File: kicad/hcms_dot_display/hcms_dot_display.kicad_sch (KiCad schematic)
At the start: 37 parts

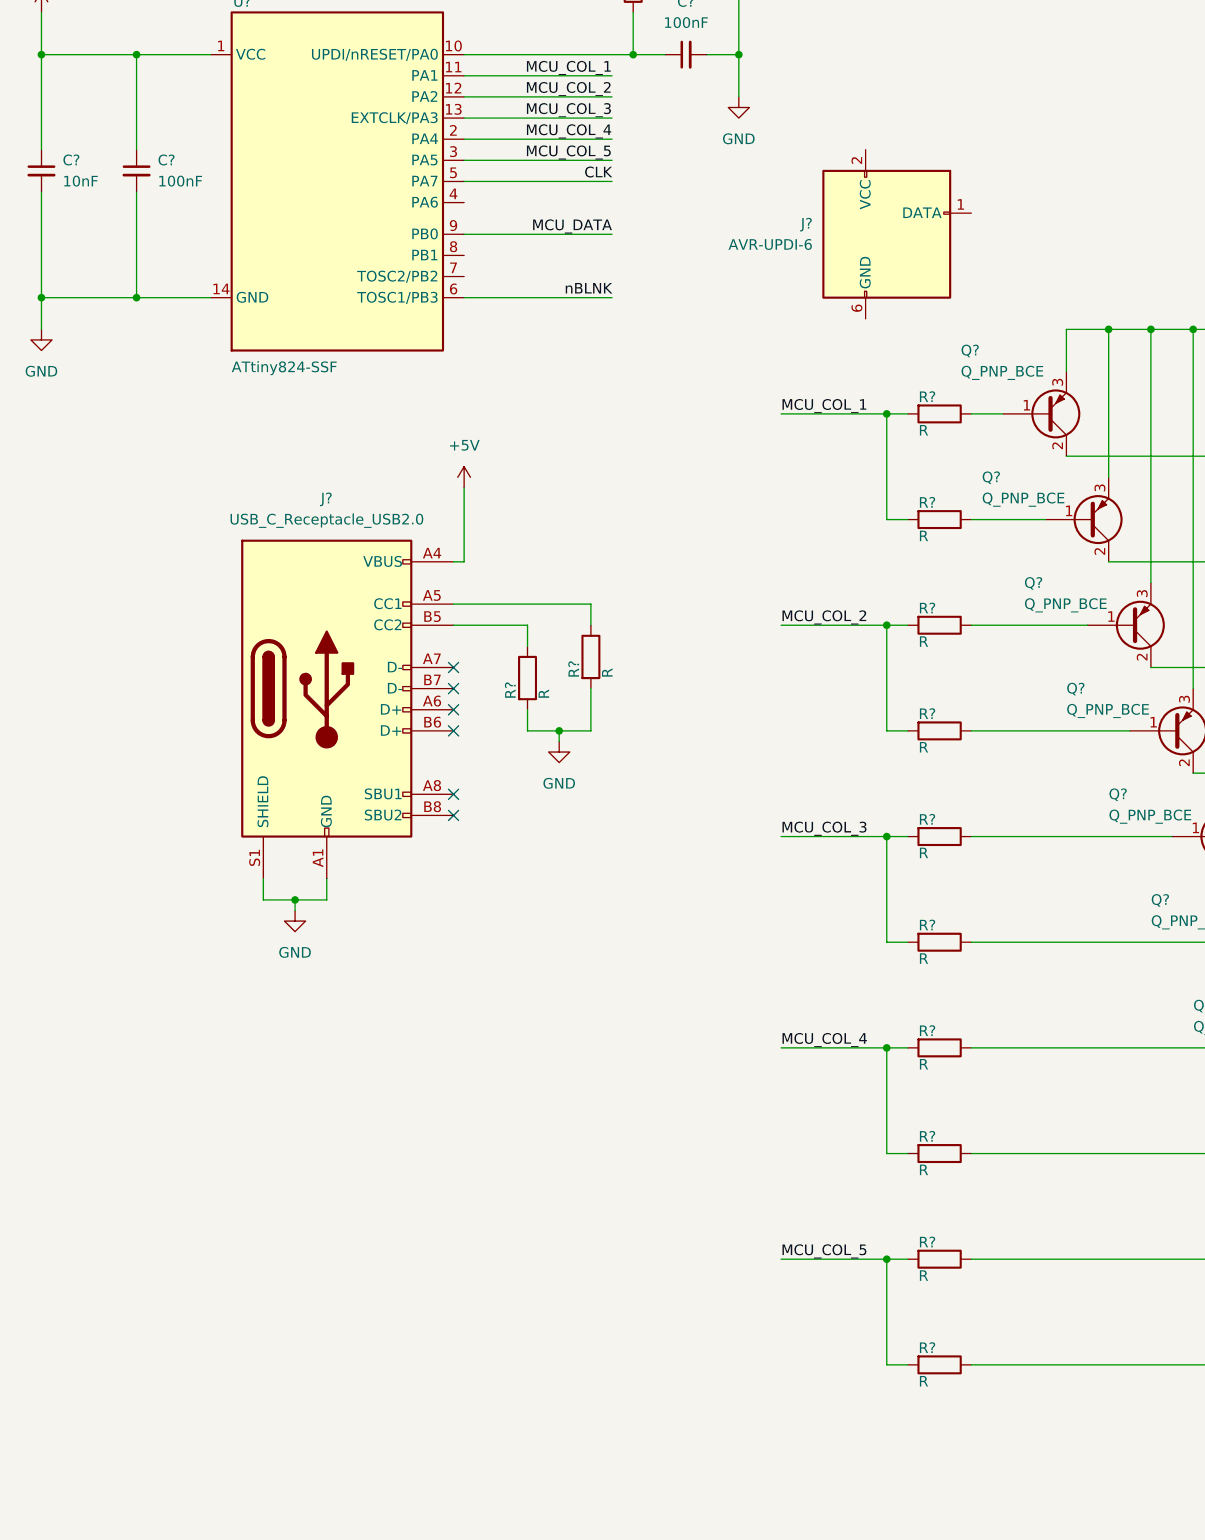
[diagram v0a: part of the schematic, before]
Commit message: battery dying
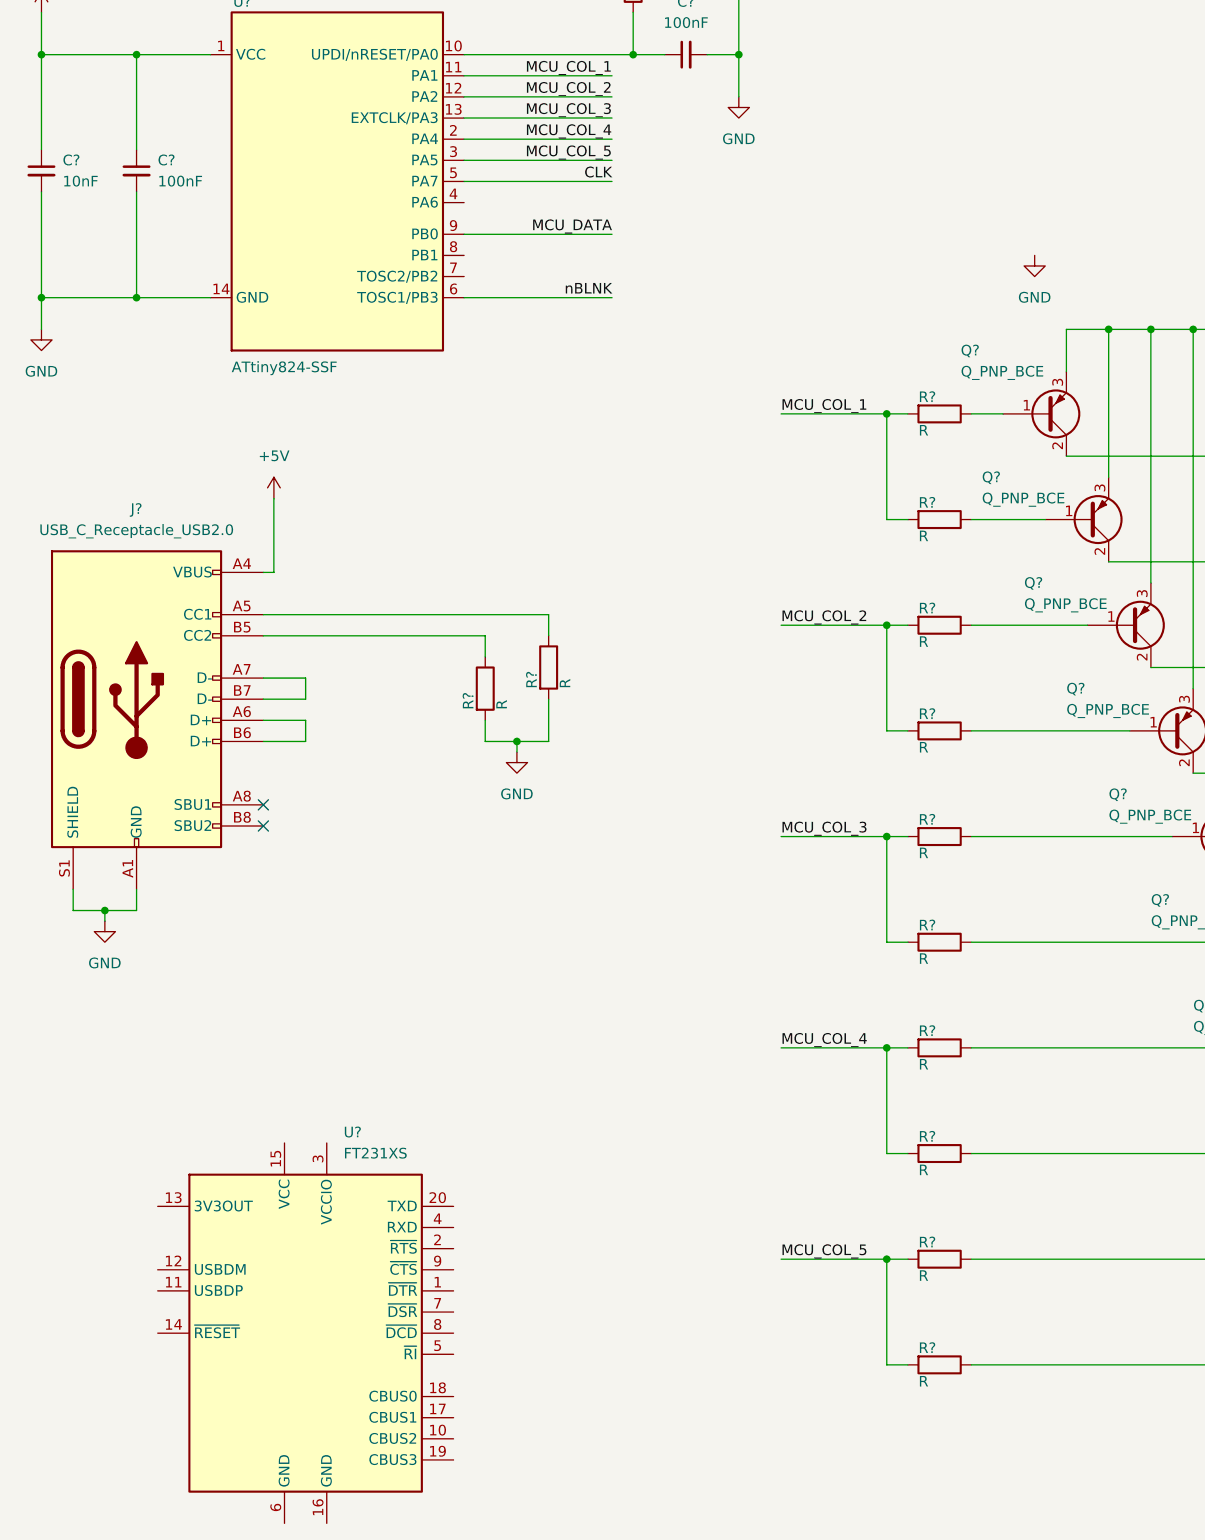
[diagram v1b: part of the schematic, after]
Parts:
- removed J?: AVR-UPDI-6, symbol Connector:AVR-UPDI-6
- added U?: FT231XS, Package_SO:SSOP-20_3.9x8.7mm_P0.635mm, symbol Interface_USB:FT231XS
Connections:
- net at J?.A6 (D+): now also J?.B6 (D+)
- net at J?.A7 (D-): now also J?.B7 (D-)
- no-connect marks 26 -> 22
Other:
- moved on the sheet: J?, R?

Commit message: aidan
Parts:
- removed Q? (x10): Q_PNP_BCE, symbol Device:Q_PNP_BCE
- removed R?: R, symbol Device:R
- added C? (x4): (no value), symbol Device:C_Small
- added C? (x2): 100nF, symbol Device:C_Small
- added J?: Conn_01x13, symbol Connector_Generic:Conn_01x13
- added Q? (x8): Q_PMOS_DSG, symbol Device:Q_PMOS_DSG
- added Q?: (no value), symbol Device:Q_PMOS_DSG
- added R? (x3): R, symbol Device:R
- added RV?: (no value), symbol Device:R_Potentiometer
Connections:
- net +5V: now also U?.15 (VCC), C?.1, C?.1, C?.1, J?.1 (Pin_1), Q?.2 (S), Q?.2 (S), Q?.2 (S), Q?.2 (S), Q?.2 (S), Q?.2 (S), Q?.2 (S), Q?.2 (S), Q?.2 (S), RV?.1
- net A_DATA: now also J?.9 (Pin_9)
- net B_DATA: now also J?.10 (Pin_10)
- net CLK: now also J?.8 (Pin_8)
- net COL_1A: now also Q?.1 (D)
- net COL_1B: now also Q?.1 (D)
- net COL_2A: now also Q?.1 (D)
- net COL_2B: now also Q?.1 (D)
- net COL_3A: now also Q?.1 (D)
- net COL_3B: now also Q?.1 (D)
- net COL_4A: now also Q?.1 (D)
- net COL_5A: now also Q?.1 (D)
- net DAISY_A_DATA: now also J?.11 (Pin_11)
- net DAISY_B_DATA: now also J?.12 (Pin_12)
- net GND: now also U?.16 (GND), U?.6 (GND), C?.2, C?.2, C?.2, C?.2, C?.2, C?.2, J?.13 (Pin_13), RV?.3
- net MCU_COL_1: now also J?.2 (Pin_2)
- net MCU_COL_2: now also J?.3 (Pin_3)
- net MCU_COL_3: now also J?.4 (Pin_4)
- net MCU_COL_4: now also J?.5 (Pin_5)
- net MCU_COL_5: now also J?.6 (Pin_6)
- net nBLNK: now also J?.7 (Pin_7)
- net at R?.1: now also Q?.3 (G) (x9)
- net at U?.11 (USBDP): now also R?.1
- net at U?.12 (USBDM): now also R?.1
- net +3V3: now reaches U?.13 (3V3OUT)
- net +3V3: now also U?.14 (~{RESET}), U?.3 (VCCIO), C?.1
- net at U?.20 (TXD): now also R?.2
- net UPDI: now reaches U?.4 (RXD)
- net UPDI: now also C?.1, R?.1, U?.10 (UPDI/nRESET/PA0), R?.1
- net POT: now reaches U?.4 (PA6)
- net POT: now also RV?.2
- net D+: now reaches J?.A6 (D+), J?.B6 (D+)
- net D+: now also C?.1, R?.2
- net D-: now reaches J?.A7 (D-), J?.B7 (D-)
- net D-: now also C?.1, R?.2
- no-connect marks 22 -> 32

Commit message: Reduce number of FETs, cleaned up schematic added some footprints, and starting routing
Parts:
- removed Q? (x4): Q_PMOS_DSG, symbol Device:Q_PMOS_DSG
- removed R? (x4): R, symbol Device:R
- added SW?: (no value), symbol Switch:SW_SPST
- D1: renamed from D?; value HCMS-272X -> (none)
- J1, J3: renamed from J?; value Conn_01x13 -> (none)
- J2: renamed from J?; value USB_C_Receptacle_USB2.0 -> (none)
- gave numbers to parts that had none: 33
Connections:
- net COL_1B is gone; now on net COL_1: D1.8 (COL_1)
- net COL_2B is gone; now on net COL_2: D1.2 (COL_2)
- net COL_3B is gone; now on net COL_3: D1.10 (COL_3)
- net COL_4B is gone; now on net COL_4: D1.4 (COL_4)
- net COL_5B is gone; now on net COL_5: D1.12 (COL_5)
- net +5V: now also SW?.2 (B); no longer J2.A4 (VBUS), J2.A9 (VBUS), J2.B4 (VBUS), J2.B9 (VBUS)
- net COL_1A renamed COL_1
- net COL_2A renamed COL_2
- net COL_3A renamed COL_3
- net COL_4A renamed COL_4
- net COL_5A renamed COL_5
- new net: J2.A4 (VBUS), J2.A9 (VBUS), J2.B4 (VBUS), J2.B9 (VBUS), SW?.1 (A)
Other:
- moved on the sheet: C1, C2, C3, C4, C5, C6, C7, C8, C9, D1A, D1B, J1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

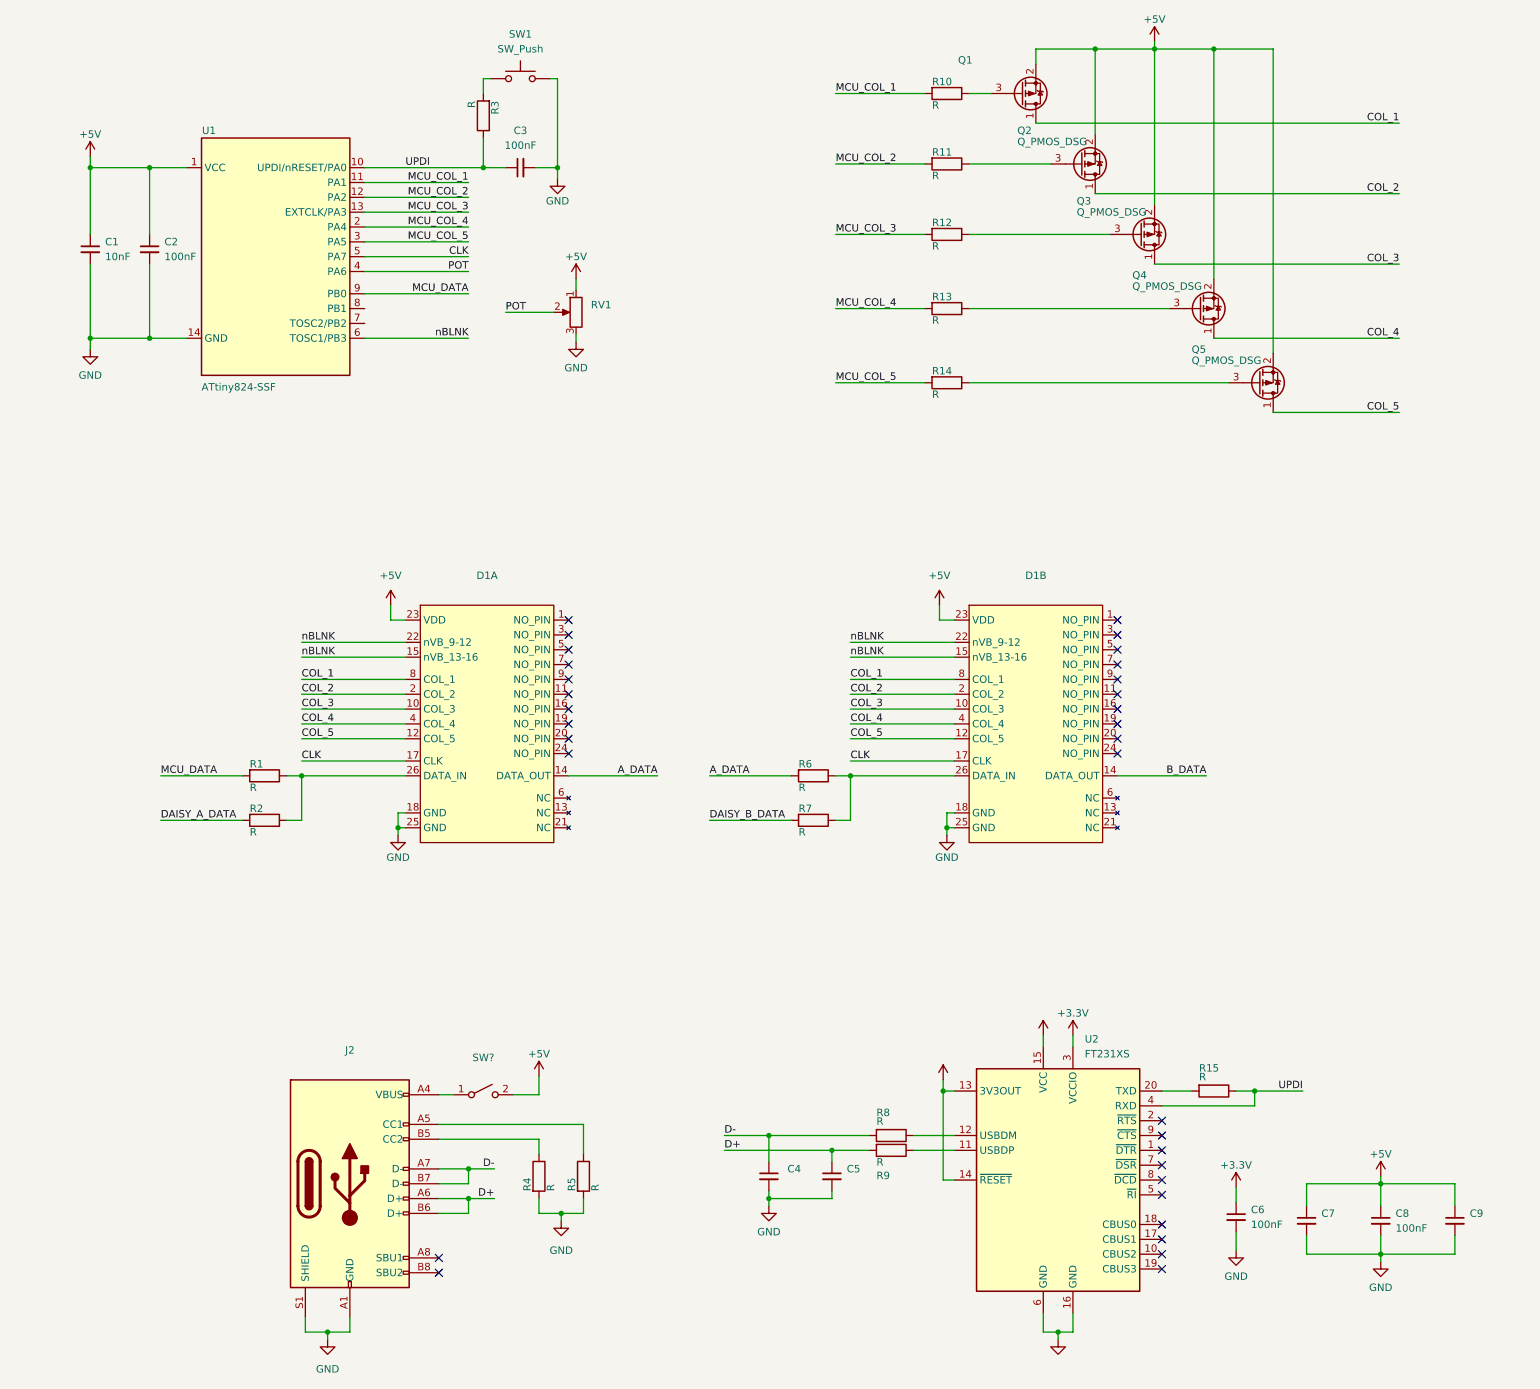
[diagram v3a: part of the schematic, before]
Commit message: Added PNs for push button and pot with basic footprints, updated some resistor values
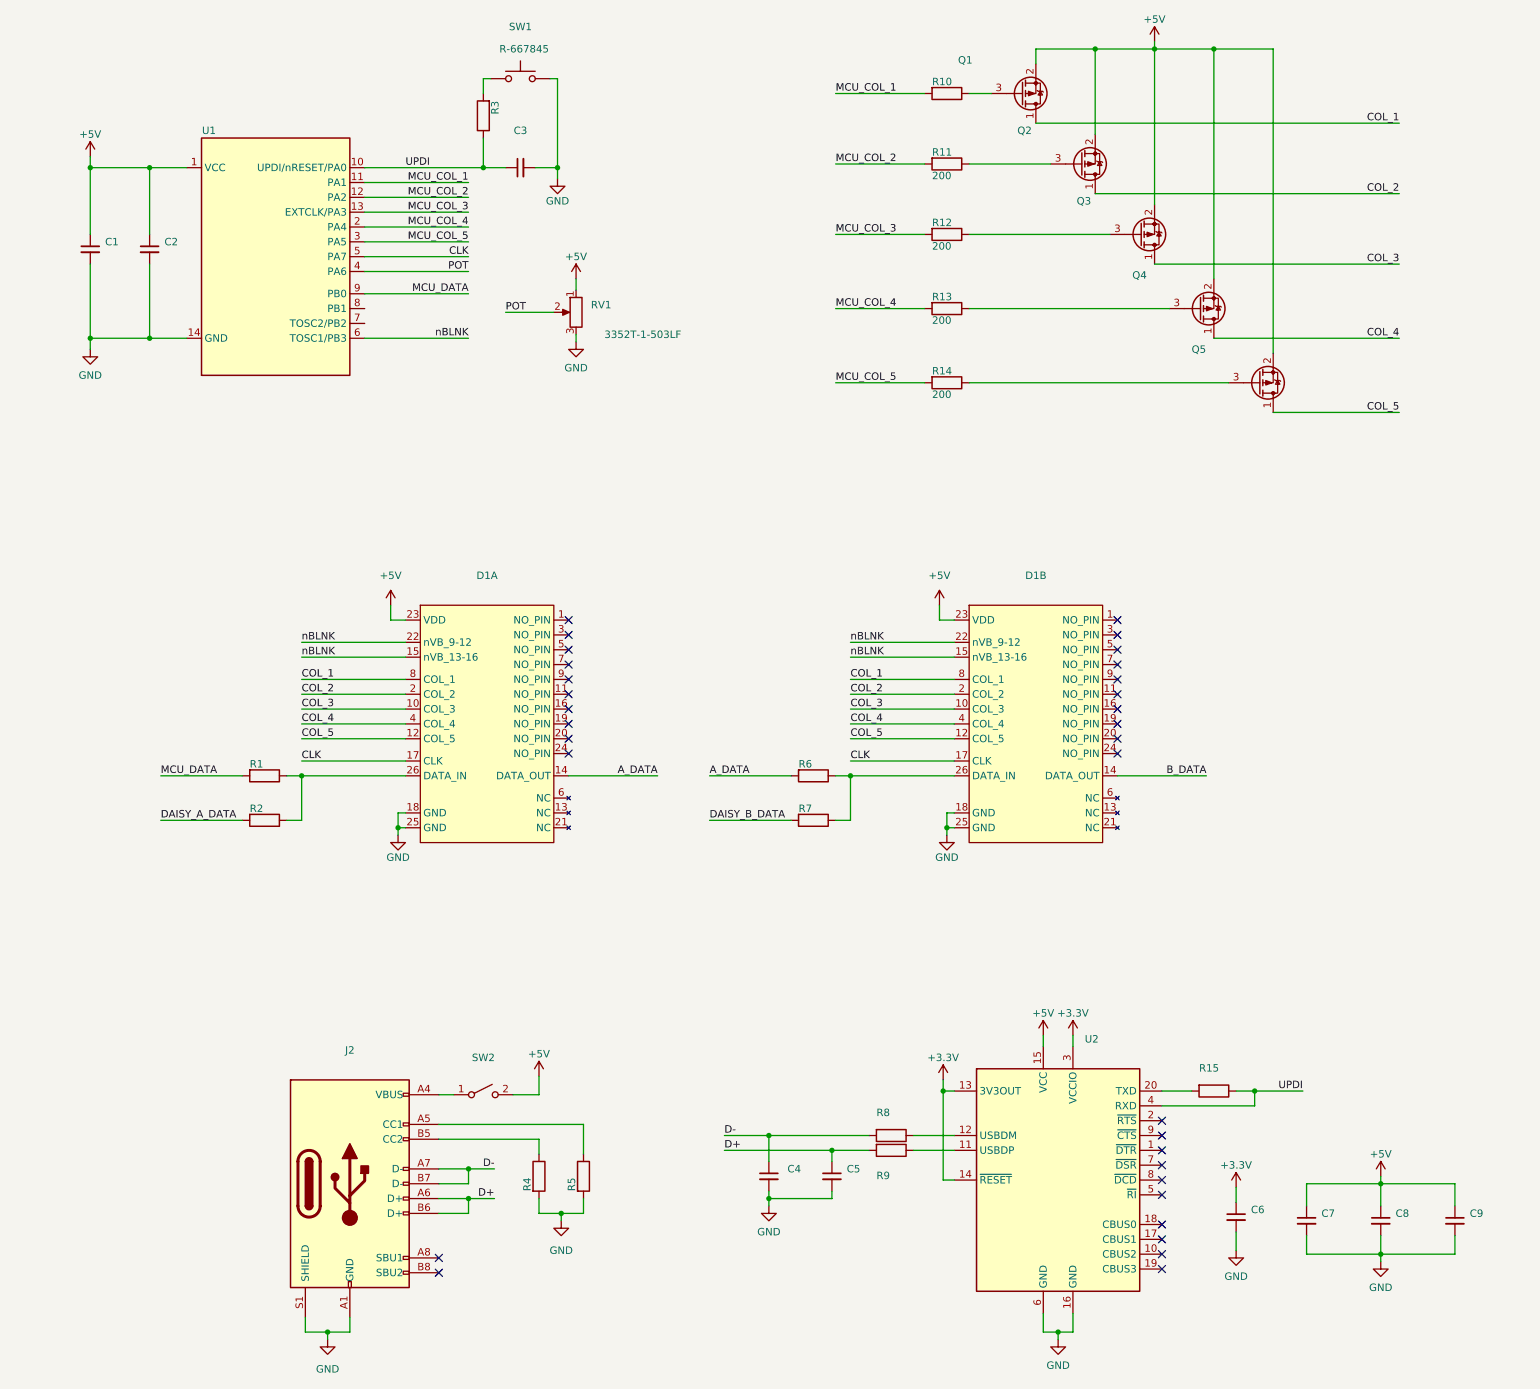
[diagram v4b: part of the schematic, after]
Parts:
- C1: value 10nF -> (none)
- C2, C3, C6, C8: value 100nF -> (none)
- Q2, Q3, Q4, Q5: value Q_PMOS_DSG -> (none)
- R1, R10, R15, R2, R3, R4, R5, R6, R7, R8, R9: value R -> (none)
- R11, R12, R13, R14: value R -> 200; footprint (none) -> Resistor_SMD:R_0603_1608Metric
- RV1: DPN (none) -> 3352T-1-503LF
- SW1: value SW_Push -> (none); DPN (none) -> R-667845
- U1: value ATtiny824-SSF -> (none); footprint Package_SO:SOIC-14_3.9x8.7mm_P1.27mm -> (none)
- U2: value FT231XS -> (none); footprint Package_SO:SSOP-20_3.9x8.7mm_P0.635mm -> (none)
- gave numbers to parts that had none: 1
